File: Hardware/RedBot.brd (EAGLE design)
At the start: 94 x 49.5 mm, 66 parts, among them U1 ATMEGA328P, U2 TB6612FNG, U3 MIC5219 5V, U4 MIC5219 3.3V, U5 FT232RLSSOP, U6 7408SE, Y1 16MHz

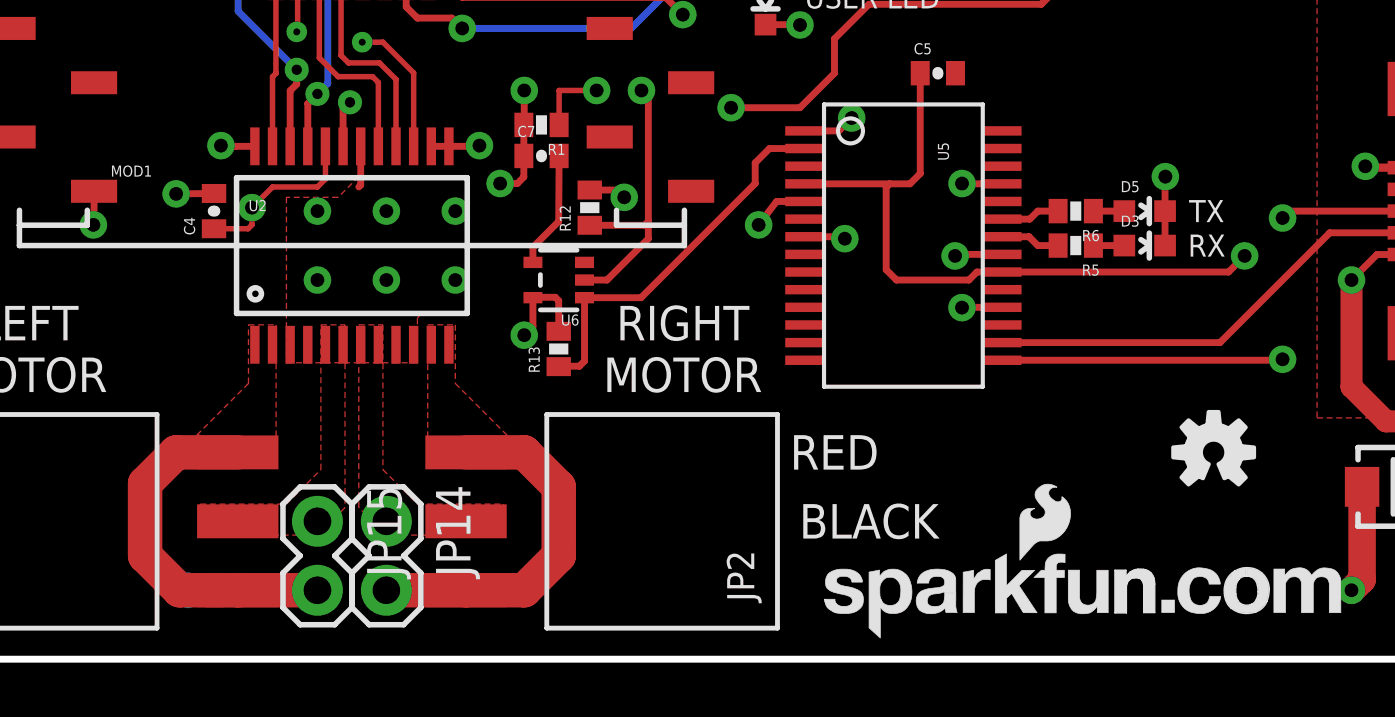
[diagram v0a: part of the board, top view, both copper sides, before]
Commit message: Fix polarity issue on FT232 LEDs
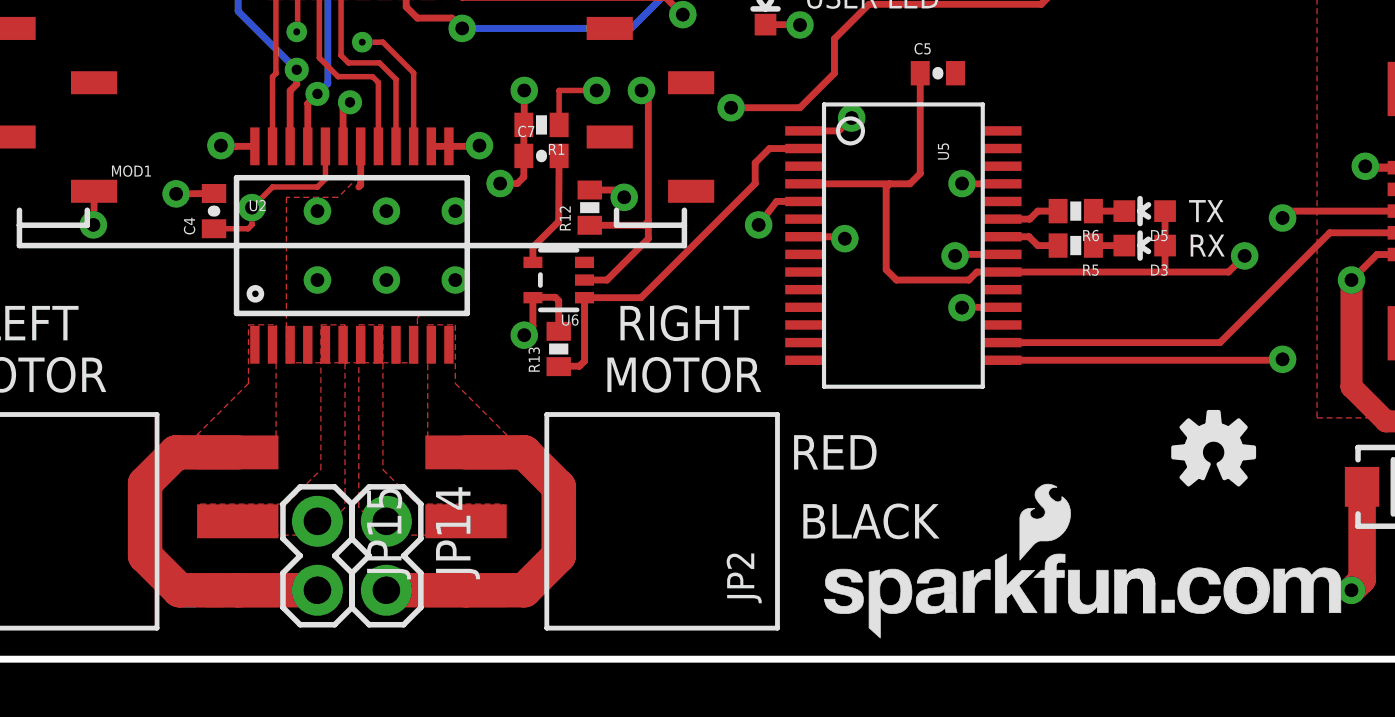
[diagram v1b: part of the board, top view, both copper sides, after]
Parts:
- turned D3 to 90 degrees
- turned D5 to 90 degrees
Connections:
- net GND: no longer D3.C, D5.C
- net N$3: now also D5.C; no longer D5.A
- net N$4: now also D3.C; no longer D3.A
- net V_USB: now also D3.A, D5.A
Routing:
- net GND: track 84.7 -> 82.2 mm, vias 44 -> 43
- net V_USB: track 43.5 -> 45.7 mm
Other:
- board text added: "v11"
- board text removed: "v10"
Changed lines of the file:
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@@
 <setting verticaltext="up"/>
 </settings>
-<grid distance="0.05" unitdist="inch" unit="inch" style="lines" multiple="1" display="yes" altdistance="0.01" altunitdist="inch" altunit="inch"/>
+<grid distance="0.05" unitdist="inch" unit="inch" style="lines" multiple="1" display="yes" altdistance="0.005" altunitdist="inch" altunit="inch"/>
 <layers>
 <layer number="1" name="Top" color="4" fill="1" visible="yes" active="yes"/>
@@
 <layer number="19" name="Unrouted" color="6" fill="1" visible="yes" active="yes"/>
 <layer number="20" name="Dimension" color="6" fill="1" visible="yes" active="yes"/>
-<layer number="21" name="tPlace" color="6" fill="1" visible="yes" active="yes"/>
-<layer number="22" name="bPlace" color="6" fill="1" visible="yes" active="yes"/>
+<layer number="21" name="tPlace" color="16" fill="1" visible="yes" active="yes"/>
+<layer number="22" name="bPlace" color="14" fill="1" visible="yes" active="yes"/>
 <layer number="23" name="tOrigins" color="15" fill="1" visible="yes" active="yes"/>
 <layer number="24" name="bOrigins" color="15" fill="1" visible="yes" active="yes"/>
-<layer number="25" name="tNames" color="7" fill="1" visible="yes" active="yes"/>
-<layer number="26" name="bNames" color="7" fill="1" visible="yes" active="yes"/>
-<layer number="27" name="tValues" color="7" fill="1" visible="yes" active="yes"/>
-<layer number="28" name="bValues" color="7" fill="1" visible="yes" active="yes"/>
-<layer number="29" name="tStop" color="7" fill="3" visible="yes" active="yes"/>
-<layer number="30" name="bStop" color="7" fill="6" visible="yes" active="yes"/>
-<layer number="31" name="tCream" color="7" fill="4" visible="yes" active="yes"/>
-<layer number="32" name="bCream" color="7" fill="5" visible="yes" active="yes"/>
-<layer number="39" name="tKeepout" color="4" fill="11" visible="yes" active="yes"/>
-<layer number="40" name="bKeepout" color="1" fill="11" visible="yes" active="yes"/>
-<layer number="41" name="tRestrict" color="4" fill="10" visible="yes" active="yes"/>
-<layer number="42" name="bRestrict" color="1" fill="10" visible="yes" active="yes"/>
-<layer number="44" name="Drills" color="7" fill="1" visible="yes" active="yes"/>
+<layer number="25" name="tNames" color="7" fill="1" visible="no" active="yes"/>
+<layer number="26" name="bNames" color="7" fill="1" visible="no" active="yes"/>
+<layer number="27" name="tValues" color="7" fill="1" visible="no" active="yes"/>
+<layer number="28" name="bValues" color="7" fill="1" visible="no" active="yes"/>
+<layer number="29" name="tStop" color="7" fill="3" visible="no" active="yes"/>
+<layer number="30" name="bStop" color="7" fill="6" visible="no" active="yes"/>
+<layer number="31" name="tCream" color="7" fill="4" visible="no" active="yes"/>
+<layer number="32" name="bCream" color="7" fill="5" visible="no" active="yes"/>
+<layer number="39" name="tKeepout" color="4" fill="11" visible="no" active="yes"/>
+<layer number="40" name="bKeepout" color="1" fill="11" visible="no" active="yes"/>
+<layer number="41" name="tRestrict" color="4" fill="10" visible="no" active="yes"/>
+<layer number="42" name="bRestrict" color="1" fill="10" visible="no" active="yes"/>
+<layer number="43" name="vRestrict" color="2" fill="10" visible="no" active="yes"/>
+<layer number="44" name="Drills" color="7" fill="1" visible="no" active="yes"/>
 <layer number="45" name="Holes" color="7" fill="1" visible="yes" active="yes"/>
-<layer number="46" name="Milling" color="3" fill="1" visible="yes" active="yes"/>
+<layer number="46" name="Milling" color="3" fill="1" visible="no" active="yes"/>
 <layer number="51" name="tDocu" color="6" fill="1" visible="yes" active="yes"/>
-<layer number="52" name="bDocu" color="7" fill="1" visible="yes" active="yes"/>
+<layer number="52" name="bDocu" color="7" fill="1" visible="no" active="yes"/>
 <layer number="3" name="Route3" color="4" fill="3" visible="no" active="no"/>
 <layer number="4" name="Route4" color="1" fill="4" visible="no" active="no"/>
@@
 <layer number="37" name="tTest" color="7" fill="1" visible="no" active="no"/>
 <layer number="38" name="bTest" color="7" fill="1" visible="no" active="no"/>
-<layer number="43" name="vRestrict" color="2" fill="10" visible="no" active="no"/>
 <layer number="47" name="Measures" color="7" fill="1" visible="no" active="no"/>
 <layer number="48" name="Document" color="7" fill="1" visible="no" active="no"/>
@@
 <text x="58.42" y="44.323" size="1.27" layer="21" font="vector" ratio="15" align="center">POWER</text>
 <text x="66.167" y="24.384" size="0.8128" layer="21" font="vector" ratio="15" align="center">USER LED</text>
-<text x="41.91" y="2.54" size="1.27" layer="16" font="vector" ratio="15" rot="MR0" align="center">v10</text>
+<text x="41.91" y="2.54" size="1.27" layer="16" font="vector" ratio="15" rot="MR0" align="center">v11</text>
 <text x="3.175" y="41.021" size="0.8128" layer="21" font="vector" ratio="15">5V</text>
 <text x="6.985" y="39.37" size="0.8128" layer="21" font="vector" ratio="15" align="center-left">GND</text>
@@
 <attribute name="PROD_ID" value="SWCH-08247" x="25.4" y="31.75" size="1.778" layer="27" font="vector" ratio="15" display="off"/>
 </element>
-<element name="D3" library="SparkFun-LED" package="LED-0603" value="GREEN" x="76.2" y="15.24" rot="R270">
-<attribute name="PROD_ID" value="DIO-00821" x="76.2" y="15.24" size="1.778" layer="27" font="vector" ratio="15" rot="R270" display="off"/>
-<attribute name="VALUE" value="GREEN" x="76.2" y="15.24" size="1.778" layer="27" font="vector" ratio="15" rot="R270" display="off"/>
+<element name="D3" library="SparkFun-LED" package="LED-0603" value="GREEN" x="76.2" y="15.24" rot="R90">
+<attribute name="PROD_ID" value="DIO-00821" x="76.2" y="15.24" size="1.778" layer="27" font="vector" ratio="15" rot="R90" display="off"/>
+<attribute name="VALUE" value="GREEN" x="76.2" y="15.24" size="1.778" layer="27" font="vector" ratio="15" rot="R90" display="off"/>
 </element>
 <element name="D4" library="SparkFun-LED" package="LED-0603" value="GREEN" x="62.23" y="24.13" rot="R180">
@@
 <attribute name="VALUE" value="1k" x="62.23" y="26.67" size="1.778" layer="27" font="vector" ratio="15" rot="R90" display="off"/>
 </element>
-<element name="D5" library="SparkFun-LED" package="LED-0603" value="GREEN" x="76.2" y="16.51" rot="R270">
-<attribute name="PROD_ID" value="DIO-00821" x="76.2" y="16.51" size="1.778" layer="27" font="vector" ratio="15" rot="R270" display="off"/>
-<attribute name="VALUE" value="GREEN" x="76.2" y="16.51" size="1.778" layer="27" font="vector" ratio="15" rot="R270" display="off"/>
+<element name="D5" library="SparkFun-LED" package="LED-0603" value="GREEN" x="76.2" y="16.51" rot="R90">
+<attribute name="PROD_ID" value="DIO-00821" x="76.2" y="16.51" size="1.778" layer="27" font="vector" ratio="15" rot="R90" display="off"/>
+<attribute name="VALUE" value="GREEN" x="76.2" y="16.51" size="1.778" layer="27" font="vector" ratio="15" rot="R90" display="off"/>
 </element>
 <element name="JP5" library="SparkFun-Connectors" package="2X3" value="AVR_SPI_PRG_6PTH" x="69.85" y="27.94" rot="R90"/>
@@
 <contactref element="JP8" pad="5"/>
 <contactref element="S4" pad="1"/>
-<contactref element="D3" pad="C"/>
-<contactref element="D5" pad="C"/>
 <contactref element="JP5" pad="6"/>
 <contactref element="D6" pad="C"/>
@@
 <wire x1="64.953" y1="15.565" x2="65.151" y2="15.494" width="0.254" layer="1"/>
 <via x="65.151" y="15.494" extent="1-16" drill="0.508"/>
-<wire x1="76.95" y1="16.51" x2="76.95" y2="15.24" width="0.254" layer="1"/>
-<wire x1="76.95" y1="16.51" x2="76.95" y2="17.387" width="0.254" layer="1"/>
-<wire x1="76.95" y1="17.387" x2="76.962" y2="17.78" width="0.254" layer="1"/>
-<via x="76.962" y="17.78" extent="1-16" drill="0.508"/>
 <wire x1="70.966" y1="17.515" x2="69.48" y2="17.515" width="0.254" layer="1"/>
 <wire x1="69.48" y1="17.515" x2="69.469" y2="17.526" width="0.254" layer="1"/>
@@
 <contactref element="U5" pad="4"/>
 <contactref element="D2" pad="A"/>
-<wire x1="70.966" y1="14.265" x2="79.289" y2="14.265" width="0.254" layer="1"/>
+<wire x1="70.966" y1="14.265" x2="76.962" y2="14.265" width="0.254" layer="1"/>
+<wire x1="76.962" y1="14.265" x2="79.289" y2="14.265" width="0.254" layer="1"/>
 <wire x1="70.966" y1="14.265" x2="70.018" y2="14.265" width="0.254" layer="1"/>
 <wire x1="70.018" y1="14.265" x2="69.723" y2="13.97" width="0.254" layer="1"/>
@@
 <wire x1="66.675" y1="14.351" x2="66.675" y2="17.388" width="0.254" layer="1"/>
 <wire x1="66.675" y1="17.388" x2="66.802" y2="17.515" width="0.254" layer="1"/>
+<contactref element="D3" pad="A"/>
+<contactref element="D5" pad="A"/>
+<wire x1="76.95" y1="15.24" x2="76.95" y2="14.277" width="0.254" layer="1"/>
+<wire x1="76.95" y1="14.277" x2="76.962" y2="14.265" width="0.254" layer="1"/>
+<wire x1="76.95" y1="16.51" x2="76.95" y2="15.24" width="0.254" layer="1"/>
 </signal>
 <signal name="PROGRAM_ENABLE">
@@
 <contactref element="U1" pad="20"/>
 </signal>
-<signal name="N$3">
-<contactref element="R6" pad="1"/>
-<contactref element="D5" pad="A"/>
-<wire x1="74.31" y1="16.51" x2="75.45" y2="16.51" width="0.254" layer="1"/>
-</signal>
-<signal name="N$4">
-<contactref element="R5" pad="1"/>
-<contactref element="D3" pad="A"/>
-<wire x1="74.31" y1="15.24" x2="75.45" y2="15.24" width="0.254" layer="1"/>
-</signal>
 <signal name="RXLED">
 <contactref element="R5" pad="2"/>
@@
 <wire x1="30.48" y1="40.64" x2="30.48" y2="47.879" width="1.016" layer="2"/>
 </signal>
+<signal name="N$3">
+<contactref element="D5" pad="C"/>
+<contactref element="R6" pad="1"/>
+<wire x1="74.31" y1="16.51" x2="75.45" y2="16.51" width="0.254" layer="1"/>
+</signal>
+<signal name="N$4">
+<contactref element="R5" pad="1"/>
+<contactref element="D3" pad="C"/>
+<wire x1="74.31" y1="15.24" x2="75.45" y2="15.24" width="0.254" layer="1"/>
+</signal>
 </signals>
+<errors>
+</errors>
 </board>
 </drawing>

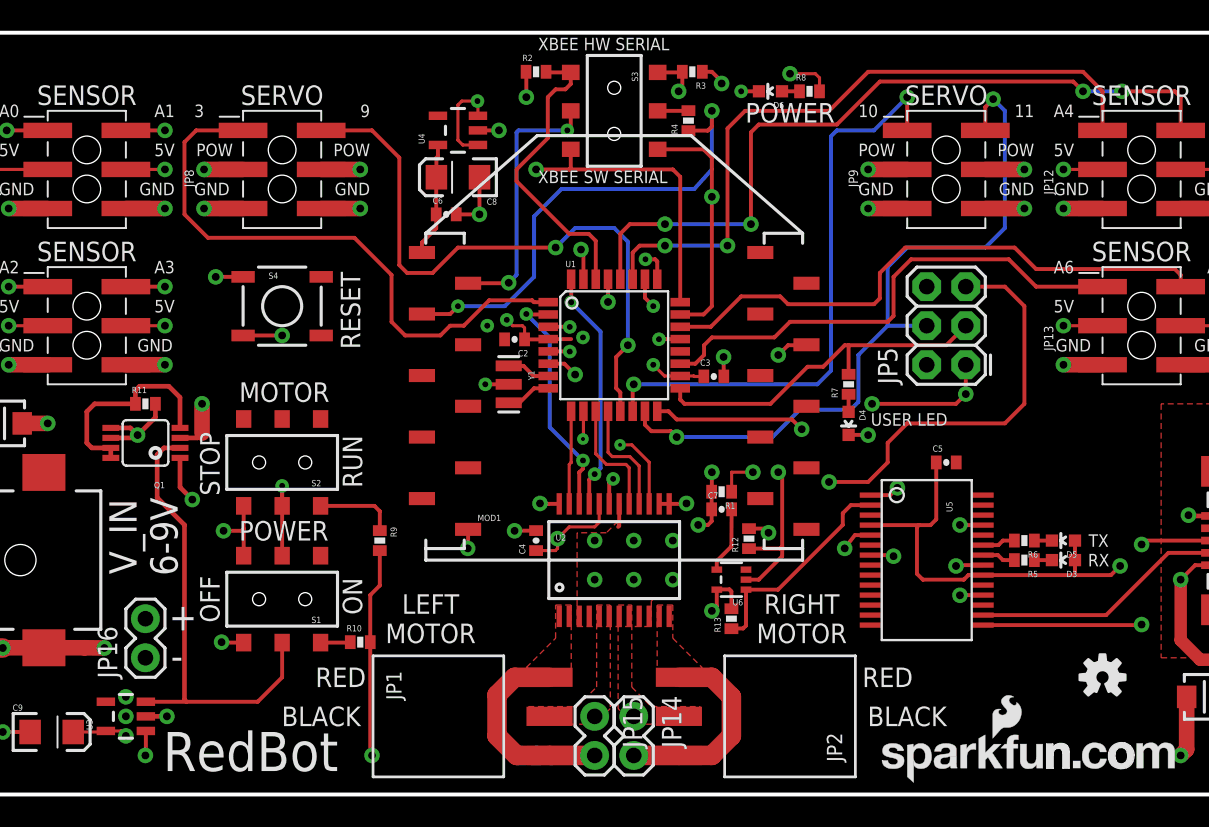
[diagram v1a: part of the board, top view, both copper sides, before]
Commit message: Update parts to 0603
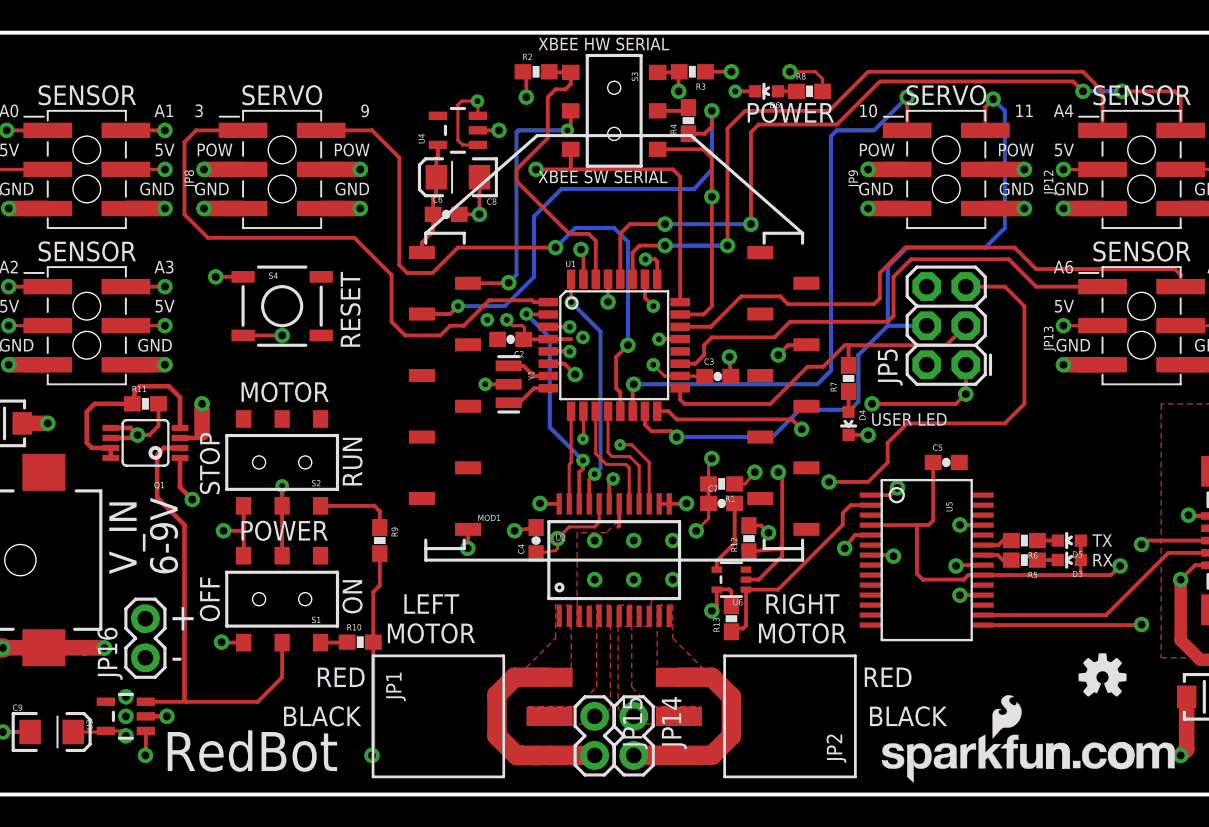
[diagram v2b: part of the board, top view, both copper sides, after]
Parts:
- C2, C3, C4, C5, C6, C7: device SparkFun-Capacitors:0402-CAP -> SparkFun-Capacitors:0603-CAP
- R1, R10, R11, R12, R13, R2, R3, R4, R5, R6, R7, R8, R9: device SparkFun-Resistors:0402-RES -> SparkFun-Resistors:0603-RES
- moved R1 0.51 mm to (54.0, 20.2)
- moved D3 0.38 mm to (76.6, 15.2)
- moved D5 0.38 mm to (76.6, 16.5)
- moved C7 0.38 mm to (54.0, 18.9)
- moved R7 0.38 mm to (62.2, 27.1)
- moved C2 0.25 mm to (40.3, 29.6)
- moved C3 0.25 mm to (53.7, 27.2)
- moved D6 0.25 mm to (56.9, 45.7)
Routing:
- net FT232_RXI: track 43.4 -> 42.5 mm
- net 5V: track 62.1 -> 61.4 mm
- net SCK: track 23.4 -> 22.8 mm
- net V_BATT: track 80.8 -> 81.3 mm
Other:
- board text added: "v12"
- board text removed: "v11"
